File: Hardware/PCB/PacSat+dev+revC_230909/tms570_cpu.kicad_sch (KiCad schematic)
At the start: 28 parts, among them J2 CONN_02X05, U2 TMS570LS0914PGE

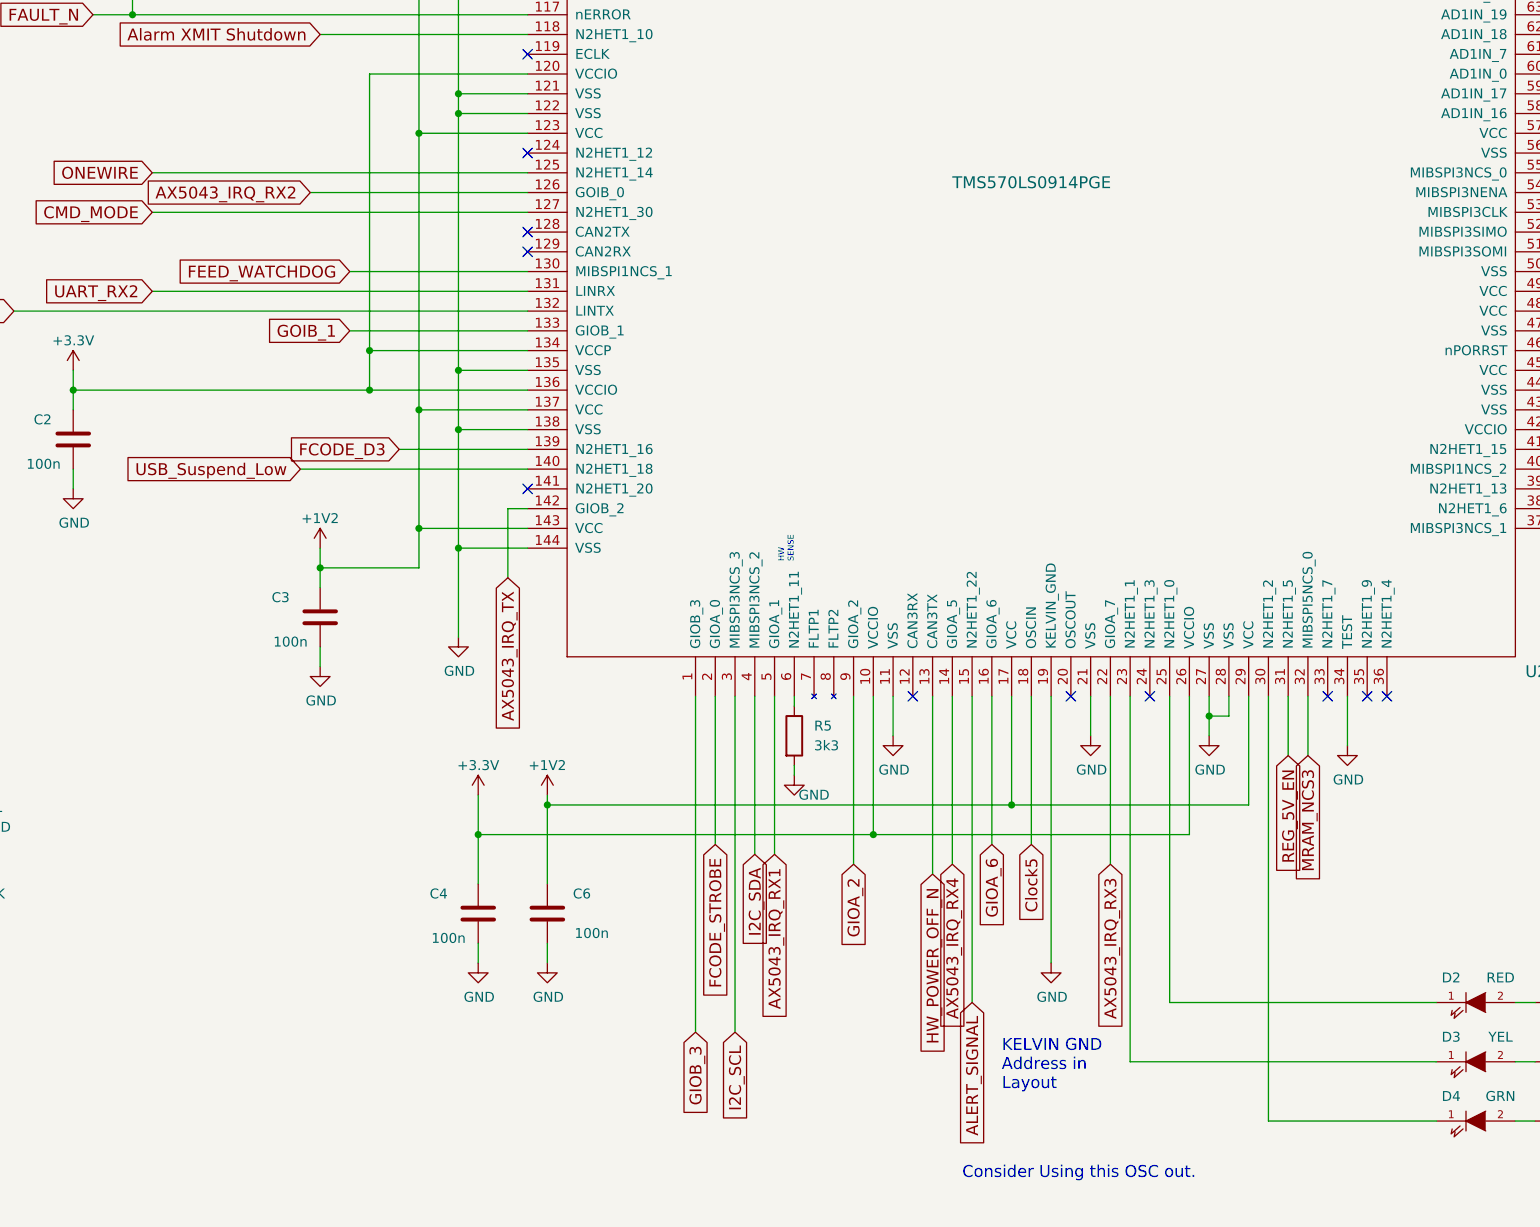
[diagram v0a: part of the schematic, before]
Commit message: Changed schematic to add Select lines for each AX5043 on the CPU.
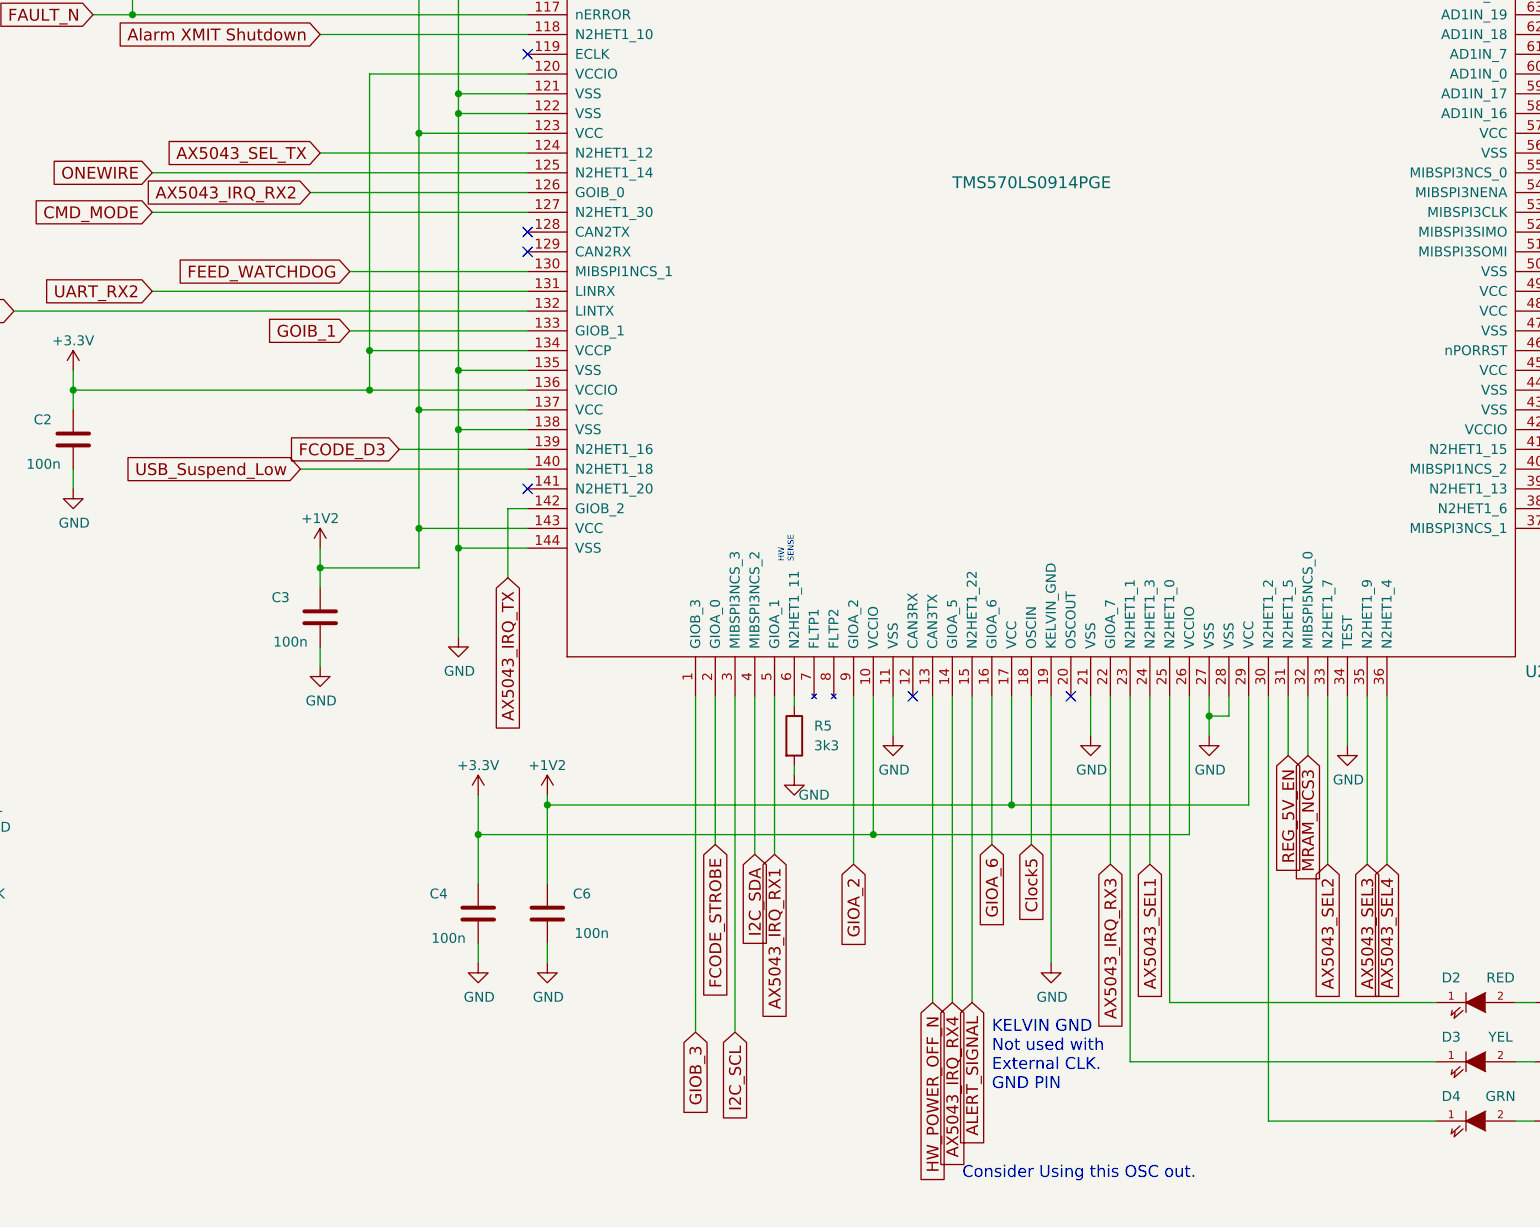
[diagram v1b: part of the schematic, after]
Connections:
- net AX5043_SEL_TX: now reaches U2.124 (N2HET1_12)
- net AX5043_SEL1: now reaches U2.24 (N2HET1_3)
- net AX5043_SEL2: now reaches U2.33 (N2HET1_7)
- net AX5043_SEL3: now reaches U2.35 (N2HET1_9)
- net AX5043_SEL4: now reaches U2.36 (N2HET1_4)
- no-connect marks 35 -> 30
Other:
- note added: "KELVIN GND Not used with External CLK. GND PIN"
- note removed: "KELVIN GND Address in Layout"
